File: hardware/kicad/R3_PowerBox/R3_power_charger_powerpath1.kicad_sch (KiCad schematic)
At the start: 44 parts, among them J7 USB-C POWER INPUT, U7 TPS2121RUXR, U8 BQ25798RQM

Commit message: Finalize R3 PowerBox pre-placement corrections
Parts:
- removed R70, R71: 5.1k Rd / 5V FALLBACK, Resistor_SMD:R_0603_1608Metric, symbol R3_POWER_GEN:R
- added C100: 100nF/25V VBUS LOCAL, Capacitor_SMD:C_0402_1005Metric, symbol R3_POWER_GEN:C
- added C101, C102, C103: 10uF/25V VBUS LOCAL, Capacitor_SMD:C_1206_3216Metric, symbol R3_POWER_GEN:C
- added C104: 1uF VREG_1V2, Capacitor_SMD:C_0603_1608Metric, symbol R3_POWER_GEN:C
- added C105: 1uF VREG_2V7, Capacitor_SMD:C_0603_1608Metric, symbol R3_POWER_GEN:C
- added C106: 4.7uF/25V PD VDD, Capacitor_SMD:C_0603_1608Metric, symbol R3_POWER_GEN:C
- added D4: ESDA25W CC ESD / P1,P2=CC P3=GND, Package_TO_SOT_SMD:SOT-323_SC-70, symbol Device:D_TVS_Dual_AAC
- added R83: 10k ALERT PU, Resistor_SMD:R_0603_1608Metric, symbol R3_POWER_GEN:R
- added R84: 10k PDO3 OK PU, Resistor_SMD:R_0603_1608Metric, symbol R3_POWER_GEN:R
- added R85: 0R PD VDD FEED, Resistor_SMD:R_0603_1608Metric, symbol R3_POWER_GEN:R
- added TP31: USB_CC1, TestPoint:TestPoint_Plated_Hole_D2.0mm, symbol R3_POWER_GEN:TP
- added TP32: USB_CC2, TestPoint:TestPoint_Plated_Hole_D2.0mm, symbol R3_POWER_GEN:TP
- added TP33: USB_VBUS_PROT, TestPoint:TestPoint_Plated_Hole_D2.0mm, symbol R3_POWER_GEN:TP
- added TP34: PD_VDD, TestPoint:TestPoint_Plated_Hole_D2.0mm, symbol R3_POWER_GEN:TP
- added TP35: PD_VREG_2V7, TestPoint:TestPoint_Plated_Hole_D2.0mm, symbol R3_POWER_GEN:TP
- added TP36: PD_ALERT_N, TestPoint:TestPoint_Plated_Hole_D2.0mm, symbol R3_POWER_GEN:TP
- added TP37: PM_I2C_SCL, TestPoint:TestPoint_Plated_Hole_D2.0mm, symbol R3_POWER_GEN:TP
- added TP38: PM_I2C_SDA, TestPoint:TestPoint_Plated_Hole_D2.0mm, symbol R3_POWER_GEN:TP
- added U10: STUSB4500QTR, Package_DFN_QFN:QFN-24-1EP_4x4mm_P0.5mm_EP2.7x2.7mm, symbol Interface_USB:STUSB4500QTR
- D3: value SMBJ15A VBUS TVS -> SMBJ13A / 13V VRWM USB VBUS
- R76: value 127k ILIM TOP -> 243k ILIM TOP / DEFAULT 0.50A
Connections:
- net N$11 is gone; now on net N$10: R75.1, U8.20 (PROG)
- net +3V3_D: now also R83.2, R84.2
- net CHARGER_IN: now also C100.1, C101.1, C102.1, C103.1
- net DGND: now also C100.2, C101.2, C102.2, C103.2, C104.2, C105.2, C106.2, D4.3 (common), U10.10 (GND), U10.12 (ADDR0), U10.13 (ADDR1), U10.22 (VSYS), U10.25 (GND), U10.6 (RESET)
- net N$10: no longer C89.1, U8.24 (SDRV)
- net N$5: now also C72.1, U7.11 (SS); no longer R73.1, U7.10 (ILIM)
- net N$6: now also R74.2, U8.18 (BATP); no longer C72.1, U7.11 (SS)
- net N$7: now also C74.1, U8.4 (BTST1); no longer R74.2, U8.18 (BATP)
- net N$8: now also C75.1, U8.19 (BTST2); no longer C74.1, U8.4 (BTST1)
- net N$9: now also C89.1, U8.24 (SDRV); no longer C75.1, U8.19 (BTST2)
- net PM_I2C_SCL: now also TP37.1, U10.7 (SCL)
- net PM_I2C_SDA: now also TP38.1, U10.8 (SDA)
- net USB_CC1: now also D4.1 (A1), TP31.1, U10.1 (CC1DB), U10.2 (CC1)
- net USB_CC2: now also D4.2 (A2), TP32.1, U10.4 (CC2), U10.5 (CC2DB)
- net USB_VBUS_PROT: now also R85.1, TP33.1, U10.18 (VBUS_VS_DISCH)
- new net N$4: R73.1, U7.10 (ILIM)
- new net PD_ALERT_N: R83.1, TP36.1, U10.19 (ALERT)
- new net PD_CONTRACT_12V_N: R84.1, U10.14 (POWER_OK3)
- new net PD_VDD: C106.1, R85.2, TP34.1, U10.24 (VDD)
- new net PD_VREG_1V2: C104.1, U10.21 (VREG_1V2)
- new net PD_VREG_2V7: C105.1, TP35.1, U10.23 (VREG_2V7)
- no-connect marks 9 -> 16
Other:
- moved on the sheet: C70, C71, C72, C73, C74, C75, C76, C77, C78, C79, C80, C81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

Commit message: Finalize R3 PowerBox pre-routing placement
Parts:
- F2: value USB INPUT 2.5A PTC / TBD -> MF-MSMF260/16X-2 2.6A/16V PPTC
- F3: value SYSTEM PTC 2.0A@60C TARGET / TBD -> MF-MSMF250/16X-2 2.5A/16V PPTC
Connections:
- net USB_SHIELD: now also J7.SH (SHIELD); no longer J7.S1 (SHIELD)
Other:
- moved on the sheet: R72, R83

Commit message: Finalize R3 PowerBox user power controls
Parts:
- added D5: LTST-C190KRKT RED / CHG, LED_SMD:LED_0603_1608Metric, symbol Device:LED
- added D7: BAT54WS-7-F STAT ISOLATION, Diode_SMD:D_SOD-323, symbol Device:D_Schottky
- added R104: 2.2k CHG LED / ~1.3mA, Resistor_SMD:R_0603_1608Metric, symbol R3_POWER_GEN:R
- added SW2: QON SERVICE / TL3305AF160QG, Button_Switch_SMD:SW_SPST_TL3305A, symbol Switch:SW_Push
- added TP39: QON_SERVICE, TestPoint:TestPoint_Plated_Hole_D2.0mm, symbol R3_POWER_GEN:TP
- R80: value 10k STAT PU -> 10k CHARGE_STATUS PU
- U7: footprint Package_DFN_QFN:Texas_VQFN-HR-12_2x2.5mm_P0.5mm_ThermalVias -> Package_DFN_QFN:Texas_VQFN-HR-12_2x2.5mm_P0.5mm
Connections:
- net CHARGE_STATUS: now also D7.2 (A); no longer U8.1 (STAT)
- net CHG_REGN: now also R104.1
- net DGND: now also SW2.2
- net QON_SERVICE: now reaches U8.12 (QON)
- net QON_SERVICE: now also SW2.1, TP39.1
- new net BQ_STAT_RAW: D5.1 (K), D7.1 (K), U8.1 (STAT)
- new net CHARGE_LED_A: D5.2 (A), R104.2
- no-connect marks 16 -> 15
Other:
- moved on the sheet: C100, C73, R81, R82

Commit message: Finish R3 PowerBox routing checkpoint F and verification
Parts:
- L3: value 1.0uH >=6A / MPN TBD -> SRP7028A-1R0M 1uH
- TP31, TP32: footprint TestPoint:TestPoint_Plated_Hole_D2.0mm -> R3_Power:TestPoint_CC_D0.6mm

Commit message: Rev.A review fixes: initial schematic and component corrections
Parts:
- added R106: 1k VBUS DISCH LIMIT, Resistor_SMD:R_0603_1608Metric, symbol R3_POWER_GEN:R
- C106: value 4.7uF/25V PD VDD -> 1uF/25V PD VDD
- C71: value 10uF/25V USB -> 4.7uF/25V USB
- C89: value 1nF SDRV -> 1nF/50V C0G SDRV
- F2: value MF-MSMF260/16X-2 2.6A/16V PPTC -> 2920L260/33DR 2.6A/33V; footprint Fuse:Fuse_1812_4532Metric_Pad1.30x3.40mm_HandSolder -> Fuse:Fuse_2920_7451Metric
- J7: value USB-C POWER INPUT -> USB4105-GF-A
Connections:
- net DGND: now also D3.2 (A); no longer D3.1 (A)
- net USB_VBUS_PROT: now also D3.1 (K), R106.1; no longer D3.2 (K), U10.18 (VBUS_VS_DISCH)
- new net PD_VBUS_SENSE_DISCH: R106.2, U10.18 (VBUS_VS_DISCH)
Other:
- moved on the sheet: C103, C71, C73

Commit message: Rev.A review fixes: local charger power-stage reroute checkpoint
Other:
- moved on the sheet: C101

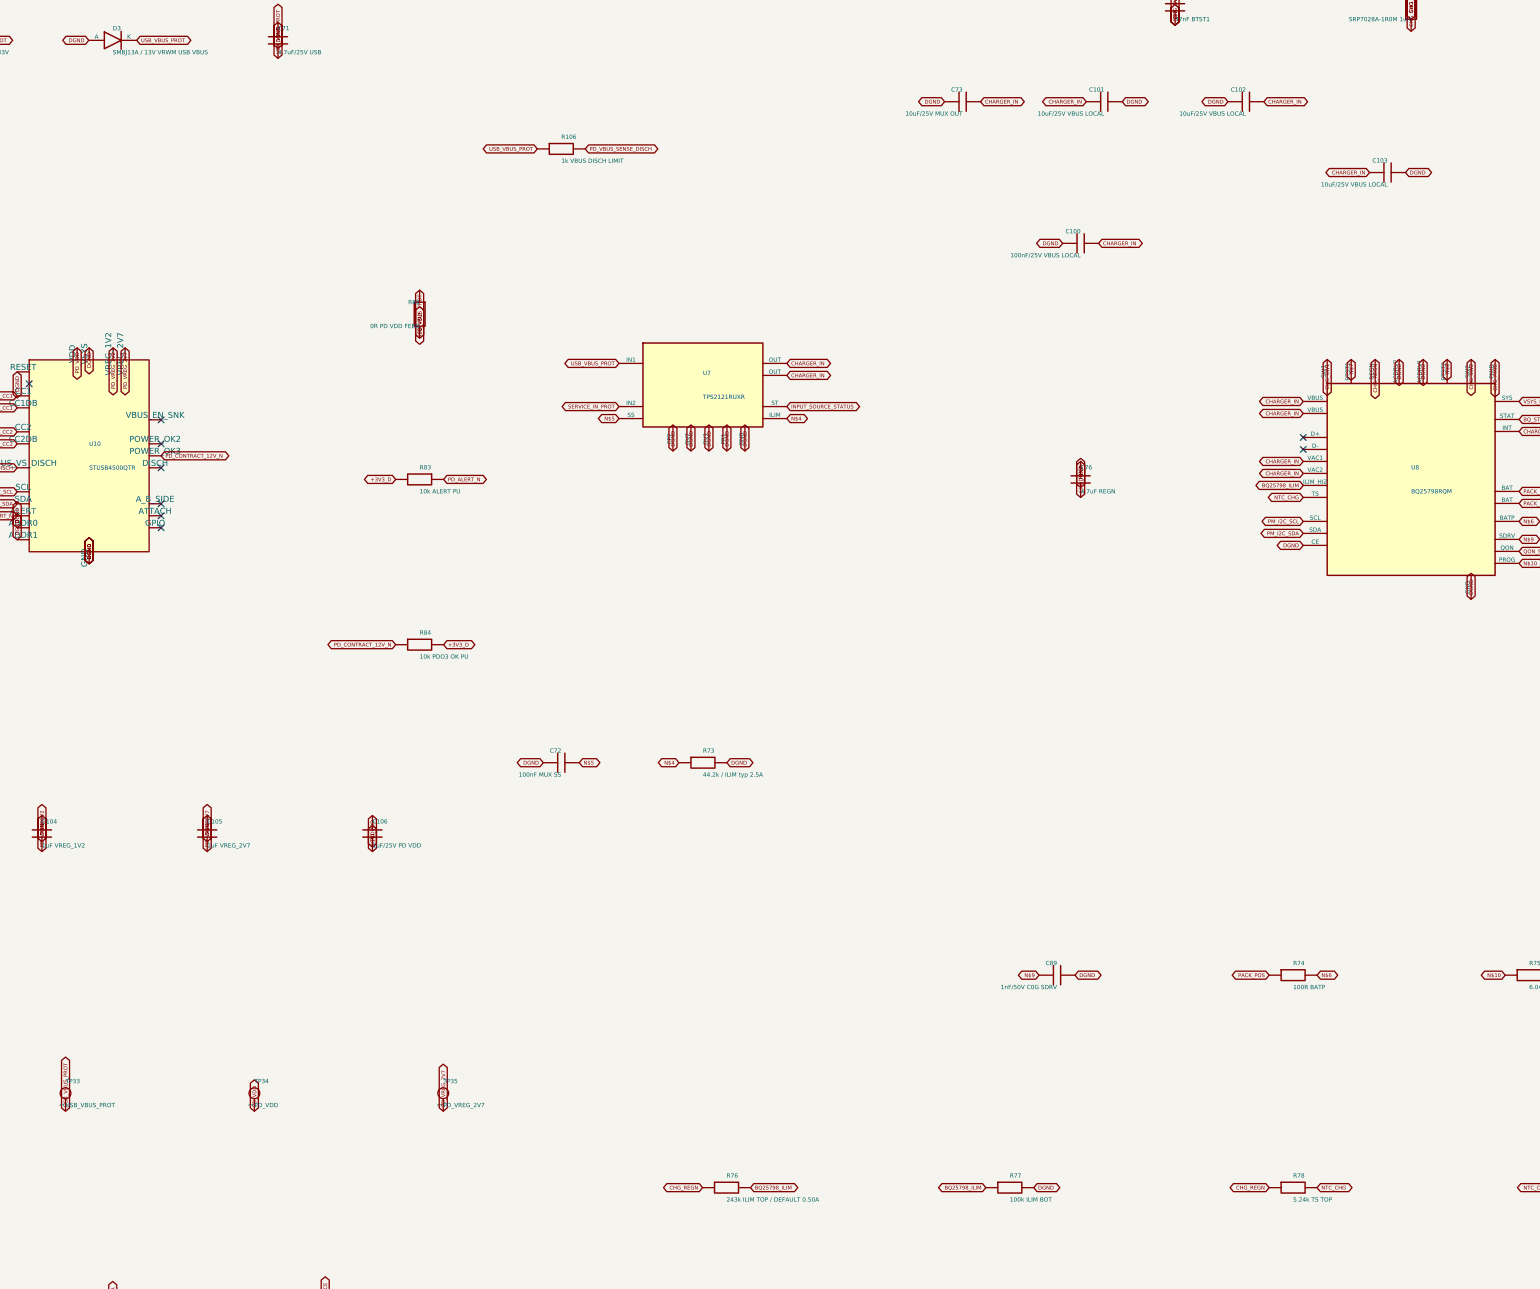
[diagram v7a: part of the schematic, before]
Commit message: Rev.A review fixes: final CAD verification and documented hardware gates
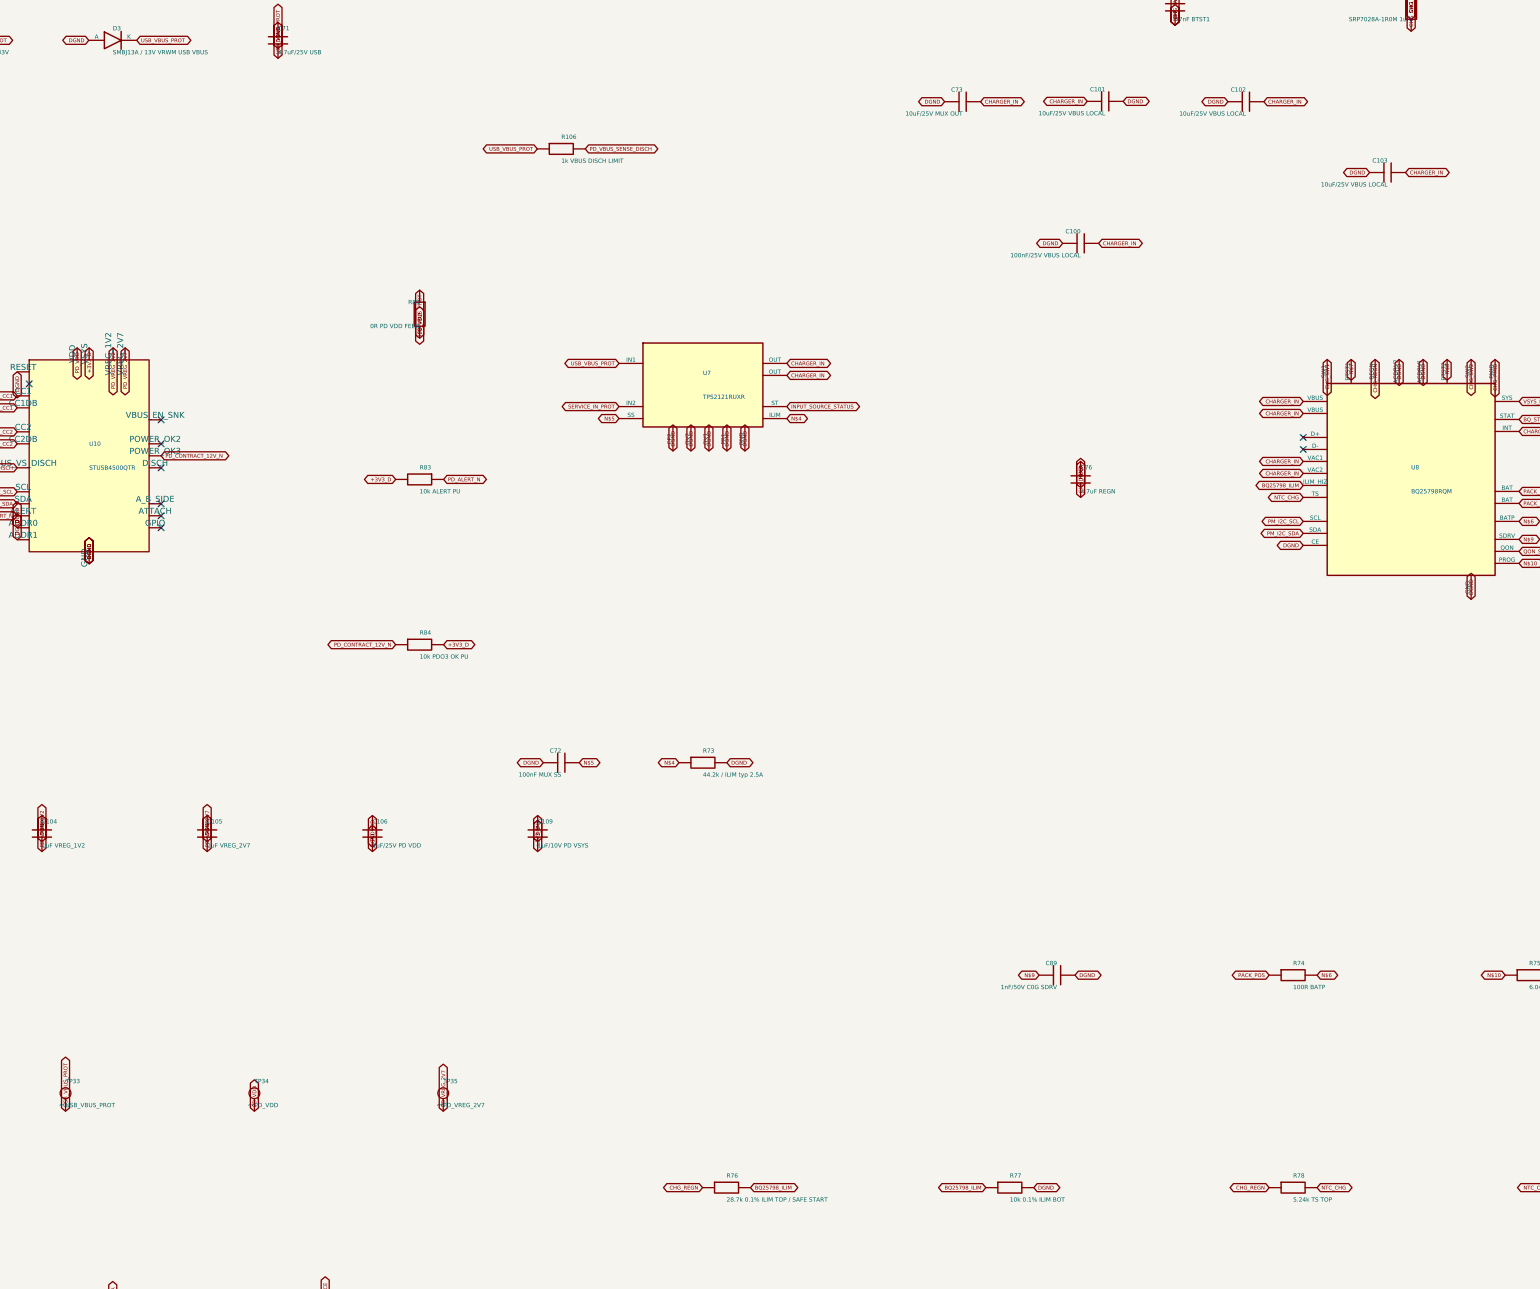
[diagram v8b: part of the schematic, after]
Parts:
- added C109: 1uF/10V PD VSYS, Capacitor_SMD:C_0402_1005Metric, symbol R3_POWER_GEN:C
- R76: value 243k ILIM TOP / DEFAULT 0.50A -> 28.7k 0.1% ILIM TOP / SAFE START
- R77: value 100k ILIM BOT -> 10k 0.1% ILIM BOT
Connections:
- net +3V3_D: now also U10.22 (VSYS), C109.1
- net DGND: now also C109.2; no longer U10.22 (VSYS)
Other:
- moved on the sheet: C103
